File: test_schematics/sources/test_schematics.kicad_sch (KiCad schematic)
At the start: 0 parts

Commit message: feat: basic I2C buses finder.
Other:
- added sheet C22: I2C Segments (i2c_segments.kicad_sch)
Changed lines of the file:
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@@
+		)
+	)
+	(sheet
+		(at 13.97 31.75)
+		(size 49.53 3.81)
+		(stroke
+			(width 0.1524)
+			(type solid)
+		)
+		(fill
+			(color 0 0 0 0.0000)
+		)
+		(property "Sheetname" "C22: I2C Segments"
+			(at 15.24 34.29 0)
+			(effects
+				(font
+					(size 1.27 1.27)
+				)
+				(justify left bottom)
+			)
+		)
+		(property "Sheetfile" "i2c_segments.kicad_sch"
+			(at 13.97 36.1446 0)
+			(effects
+				(font
+					(size 1.27 1.27)
+				)
+				(justify left top)
+			)
+		)
+		(instances
+			(project "test_schematics"
+				(path "/f327a4b6-22d9-4671-bd1f-2c46b703509e"
+					(page "4")
+				)
+			)
 		)
 	)

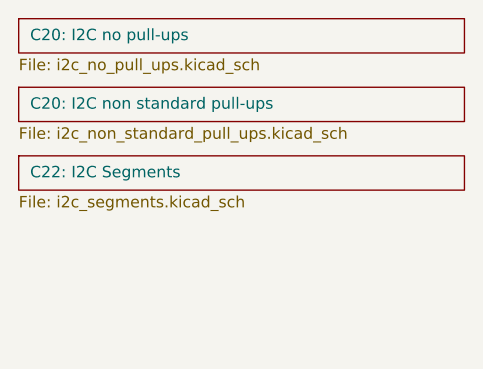
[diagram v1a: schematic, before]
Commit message: feat: find redundant pull-ups.
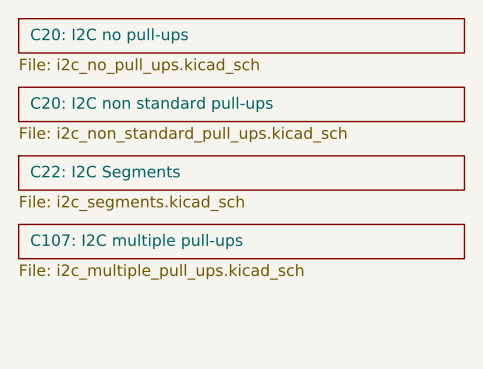
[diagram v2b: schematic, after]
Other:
- added sheet C107: I2C multiple pull-ups (i2c_multiple_pull_ups.kicad_sch)
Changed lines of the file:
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@@
+		)
+	)
+	(sheet
+		(at 13.97 39.37)
+		(size 49.53 3.81)
+		(stroke
+			(width 0.1524)
+			(type solid)
+		)
+		(fill
+			(color 0 0 0 0.0000)
+		)
+		(property "Sheetname" "C107: I2C multiple pull-ups"
+			(at 15.24 41.91 0)
+			(effects
+				(font
+					(size 1.27 1.27)
+				)
+				(justify left bottom)
+			)
+		)
+		(property "Sheetfile" "i2c_multiple_pull_ups.kicad_sch"
+			(at 13.97 43.7646 0)
+			(effects
+				(font
+					(size 1.27 1.27)
+				)
+				(justify left top)
+			)
+		)
+		(instances
+			(project "test_schematics"
+				(path "/f327a4b6-22d9-4671-bd1f-2c46b703509e"
+					(page "5")
+				)
+			)
 		)
 	)

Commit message: feat: I2C non-equal pull-ups check
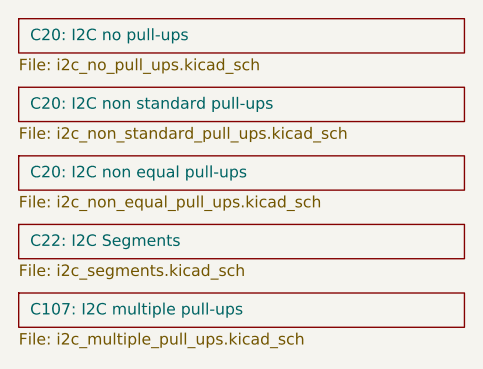
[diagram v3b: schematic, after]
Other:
- added sheet C20: I2C non equal pull-ups (i2c_non_equal_pull_ups.kicad_sch)
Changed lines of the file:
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@@
 			(color 0 0 0 0.0000)
 		)
-		(property "Sheetname" "C22: I2C Segments"
+		(property "Sheetname" "C20: I2C non equal pull-ups"
 			(at 15.24 34.29 0)
 			(effects
@@
 			)
 		)
+		(property "Sheetfile" "i2c_non_equal_pull_ups.kicad_sch"
+			(at 13.97 36.1446 0)
+			(effects
+				(font
+					(size 1.27 1.27)
+				)
+				(justify left top)
+			)
+		)
+		(instances
+			(project "test_schematics"
+				(path "/f327a4b6-22d9-4671-bd1f-2c46b703509e"
+					(page "6")
+				)
+			)
+		)
+	)
+	(sheet
+		(at 13.97 39.37)
+		(size 49.53 3.81)
+		(stroke
+			(width 0.1524)
+			(type solid)
+		)
+		(fill
+			(color 0 0 0 0.0000)
+		)
+		(property "Sheetname" "C22: I2C Segments"
+			(at 15.24 41.91 0)
+			(effects
+				(font
+					(size 1.27 1.27)
+				)
+				(justify left bottom)
+			)
+		)
 		(property "Sheetfile" "i2c_segments.kicad_sch"
-			(at 13.97 36.1446 0)
+			(at 13.97 43.7646 0)
 			(effects
 				(font
@@
 	)
 	(sheet
-		(at 13.97 39.37)
+		(at 13.97 46.99)
 		(size 49.53 3.81)
 		(stroke
@@
 		)
 		(property "Sheetname" "C107: I2C multiple pull-ups"
-			(at 15.24 41.91 0)
+			(at 15.24 49.53 0)
 			(effects
 				(font
@@
 		)
 		(property "Sheetfile" "i2c_multiple_pull_ups.kicad_sch"
-			(at 13.97 43.7646 0)
+			(at 13.97 51.3846 0)
 			(effects
 				(font
